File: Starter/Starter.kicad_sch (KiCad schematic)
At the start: 49 parts, among them J1 AudioJack, J2 Speaker, J3 UART1, J4 Pot, J5 Conn_01x08_Pin, J6 GND, J7 DACOUT, SW1 UP, SW2 LEFT, SW3 DOWN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

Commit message: schematic cleaning
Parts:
- removed J1: AudioJack, ECE319K:Jack_3.5mm_CUI_SJ1-3523N_Horizontal, symbol ECE319K:HeadphoneJack
- removed J4: Pot, ECE319K:Testpoint_1x02_P2.54mm, symbol ECE319K:Testpoint
- removed J6: GND, ECE319K:Testpoint_1x02_P2.54mm, symbol ECE319K:Testpoint
- removed TP1: 3.3V, ECE319K:Testpoint_1x02_P2.54mm, symbol ECE319K:Testpoint
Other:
- note removed: "unnecessary test point"
- moved on the sheet: C1, C2, C3, R16, R17

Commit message: fix labels and stuff
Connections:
- net GND: no longer R13.2, R14.2
- net PA12 renamed SDC_CS
- net PA13 renamed TFT_DC
- net PB15 renamed TFT_RST
- net PB6 renamed TFT_CS
- net PB7 renamed SPI_MISO
- net PB8 renamed SPI_MOSI
- net PB9 renamed SPI_SCK
- no-connect marks 0 -> 3
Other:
- note added: "do we even need this?"
- note added: "redo with proper vals"
- note removed: "cant you just use DACOUT label?"
- note removed: "speaker"
- moved on the sheet: J2

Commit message: more stuff
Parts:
- removed H1, H2, H3, H4: ~, ECE319K:MountingHole_4_40, symbol ECE319K:MountingHole
- removed R10: 12k, ECE319K:R_Axial_DIN0204_L3.6mm_D1.6mm_P7.62mm_Horizontal, symbol ECE319K:R_0.125W
- removed R5, R8: 1.5k, ECE319K:R_Axial_DIN0204_L3.6mm_D1.6mm_P7.62mm_Horizontal, symbol ECE319K:R_0.125W
- added H1, H2, H3, H4: MountingHole, symbol Mechanical:MountingHole
- R4: value 1.5k -> 750
- R7: value 1.5k -> 3k
- R9: value 12k -> 6k
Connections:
- net +3V3: now also C4.2; no longer C4.1
- net DACOUT: now also R7.1
- net GND: now also C4.1, R13.2, R14.2; no longer C4.2
- net PA22: no longer J3.3 (C), U2.J3_4 (PA22)
- net PA8: no longer J3.2 (B), U2.J1_4 (PA8)
- net PB0 renamed DAC0
- net PB1 renamed DAC1
- net PB2 renamed DAC2
- net PB3 renamed DAC3
- net PB4 renamed DAC4
- new net UART1_TX: J3.2 (B), U2.J1_4 (PA8)
- new net UART2_RX: J3.3 (C), U2.J3_4 (PA22)
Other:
- note removed: "U1_Tx"
- note removed: "U2_Rx"
- note removed: "redo with proper vals"
- note removed: "why 3v3 not 5?"
- company: The University of Texas at Austin -> Ravi Shah & Alice Di Mauro
- title: Starter Project Spring 2025 -> ECE 319H Final Project
- moved on the sheet: C4, D1, D2, D3, D4, J2, JP1, R1, R11, R12, R13, R14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

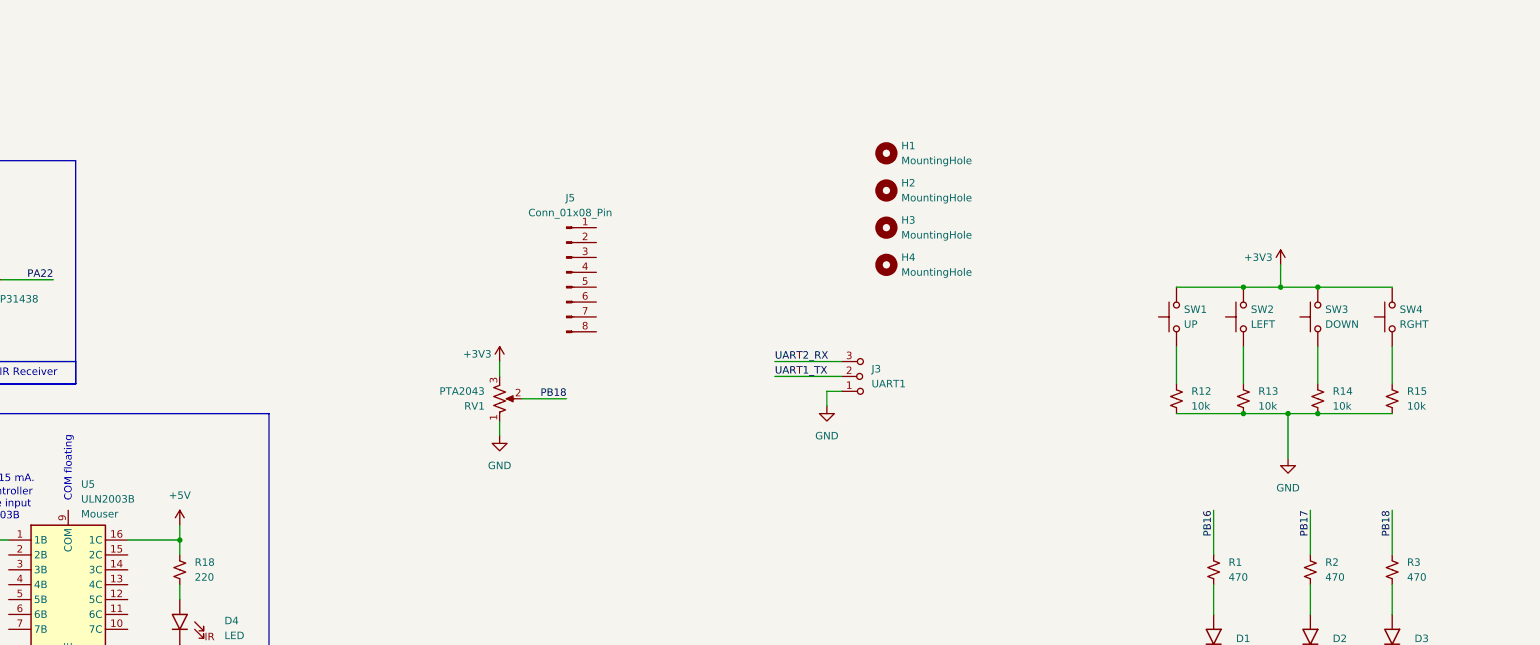
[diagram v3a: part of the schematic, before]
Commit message: add switch debounce
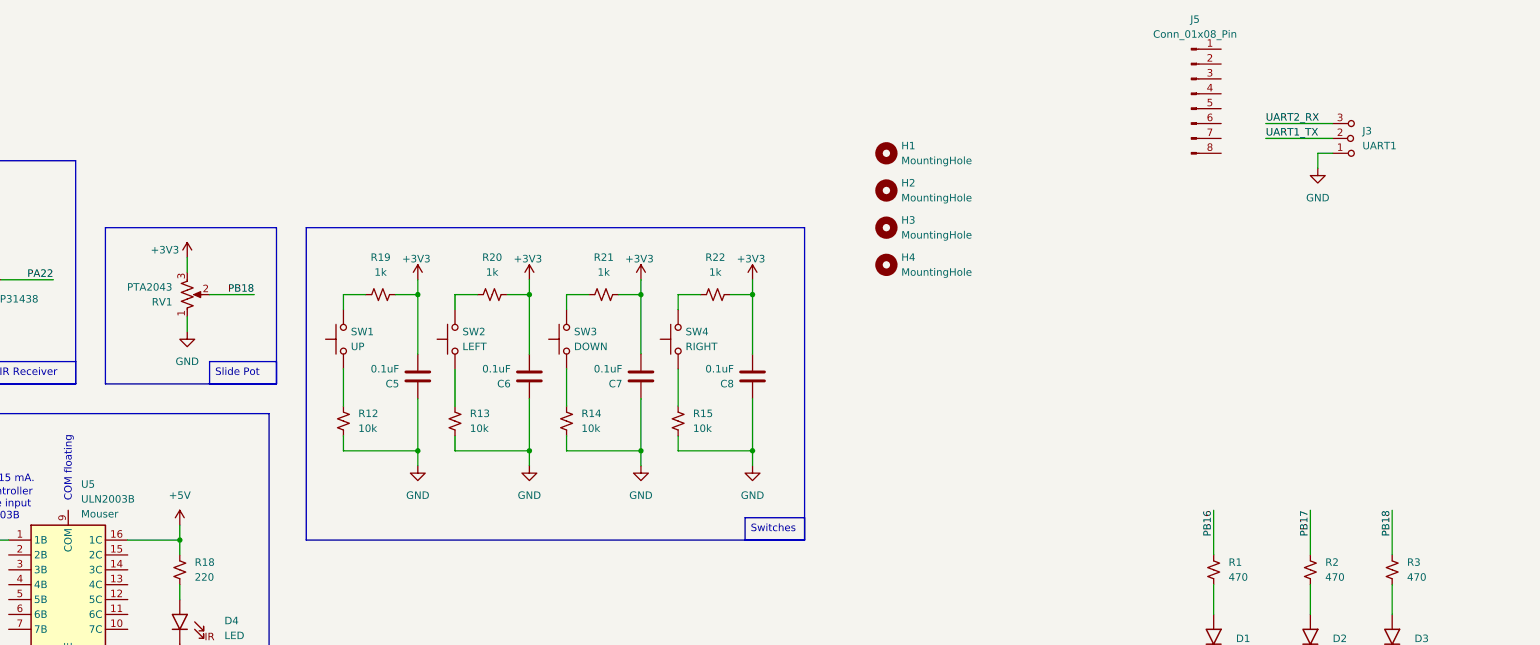
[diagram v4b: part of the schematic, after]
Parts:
- added C5, C6, C7, C8: 0.1uF, ECE319K:C_Axial_200mil, symbol ECE319K:C
- added R19, R20, R21, R22: 1k, ECE319K:R_Axial_DIN0204_L3.6mm_D1.6mm_P7.62mm_Horizontal, symbol ECE319K:R_0.125W
- SW4: value RGHT -> RIGHT
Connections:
- net +3V3: now also C5.2, C6.2, C7.2, C8.2, R19.1, R20.1, R21.1, R22.1; no longer SW1.2, SW2.2, SW3.2, SW4.2
- net GND: now also C5.1, C6.1, C7.1, C8.1
- new net: R19.2, SW1.2
- new net: R21.2, SW3.2
- new net: R22.2, SW4.2
- new net: R20.2, SW2.2
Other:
- moved on the sheet: J3, J5, R12, RV1, SW1

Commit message: speaker amp
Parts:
- removed R17: 10k, ECE319K:R_Axial_DIN0204_L3.6mm_D1.6mm_P7.62mm_Horizontal, symbol ECE319K:R_0.125W
- added D5, D6: LED, ECE319K:LED_D5.0mm, symbol ECE319K:LED
- added R23: 10k, ECE319K:R_Axial_DIN0204_L3.6mm_D1.6mm_P7.62mm_Horizontal, symbol ECE319K:R_0.125W
- added R5: TBD, ECE319K:R_Axial_DIN0204_L3.6mm_D1.6mm_P7.62mm_Horizontal, symbol ECE319K:R_0.125W
- added R8: 470, ECE319K:R_Axial_DIN0204_L3.6mm_D1.6mm_P7.62mm_Horizontal, symbol ECE319K:R_0.125W
- U3: value MCP34119P -> MCP34119D
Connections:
- net +5V: now also U3.6 (Vcc)
- net DACOUT: now also C3.1; no longer J2.1, R11.1, R4.1, R6.1, R7.1, R9.1
- net GND: now also C1.2, C2.2, U3.1 (CD), U3.7 (GND), D5.1 (K), D6.1 (K); no longer J2.2
- net PB16: no longer R1.1
- net PB17: no longer R2.1
- net PB18: no longer R3.1
- net at U3.2 (FC2): now also C2.1
- net at U3.3 (FC1): now also C1.1
- net at U3.4 (VIN): now also R16.1, R23.2
- net at U3.5 (VO1): now also J2.1, R23.1
- net at U3.8 (VO2): now also J2.2
- net at R16.2: now also C3.2
- new net: R11.1, R4.1, R6.1, R7.1, R9.1
- new net: D6.2 (A), R8.2
- new net: D5.2 (A), R5.2
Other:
- note added: "add pins and redo resistor vals based on LED datasheet"
- note removed: "check that these pins are correct?"
- moved on the sheet: C1, C2, C3, C5, C6, C7, C8, D1, D2, D3, H1, H2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

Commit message: IMU
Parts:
- added C10: 2.2nF, ECE319K:C_Axial_200mil, symbol ECE319K:C
- added C11, C9: 0.1uF, ECE319K:C_Axial_200mil, symbol ECE319K:C
- added C12: 10nF, ECE319K:C_Axial_200mil, symbol ECE319K:C
- added R10, R17: 4.7k, ECE319K:R_Axial_DIN0204_L3.6mm_D1.6mm_P7.62mm_Horizontal, symbol ECE319K:R_0.125W
- added U1: MPU-6050, Sensor_Motion:InvenSense_QFN-24_4x4mm_P0.5mm, symbol Sensor_Motion:MPU-6050
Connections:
- net PA24 is gone; now on net DAC4: U2.J3_7 (PA24)
- net PA25 is gone; now on net DAC3: U2.J1_2 (PA25)
- net PA26 is gone; now on net DAC2: U2.J1_5 (PA26)
- net PA27 is gone; now on net DAC1: U2.J1_8 (PA27)
- net PA28 is gone; now on net DAC0: U2.J4_3 (PA28)
- net +3V3: now also C11.1, C12.1, R10.1, R17.1, U1.13 (VDD), U1.8 (VLOGIC)
- net DAC0: no longer U2.J2_9 (PB0)
- net DAC1: no longer U2.J4_2 (PB1)
- net DAC2: no longer U2.J1_9 (PB2)
- net DAC3: no longer U2.J1_10 (PB3)
- net DAC4: no longer U2.J4_1 (PB4)
- net GND: now also C10.2, C11.2, C12.2, C9.2, U1.1 (CLKIN), U1.11 (FSYNC), U1.18 (GND), U1.9 (AD0)
- new net: C9.1, U1.10 (REGOUT)
- new net: C10.1, U1.20 (CPOUT)
- new net I2C_SCL: R17.2, U1.23 (SCL), U2.J1_9 (PB2)
- new net I2C_SDA: R10.2, U1.24 (SDA), U2.J1_10 (PB3)
- no-connect marks 3 -> 6
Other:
- note added: "VDD Bypass"
- note added: "VLogic Bypass"

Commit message: wow im dumb
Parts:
- added C13: 0.1uF, ECE319K:C_Axial_200mil, symbol ECE319H:C
- added D7: 1N4001, Diode_THT:D_DO-41_SOD81_P10.16mm_Horizontal, symbol Diode:1N4001
- added M1: Vibration Motor, symbol Motor:Motor_DC
- added Q1: 2N2222, symbol Simulation_SPICE:NPN
- added R24: 1k, ECE319K:R_Axial_DIN0204_L3.6mm_D1.6mm_P7.62mm_Horizontal, symbol ECE319K:R_0.125W
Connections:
- net PA22 is gone; now on net UART2_RX: U6.3 (Out)
- net PA8 is gone; now on net UART1_TX: U5.1 (1B)
- net +3V3: now also SW1.2, SW2.2, SW3.2, SW4.2, C13.1, D7.1 (K), M1.1 (+); no longer C5.2, C6.2, C7.2, C8.2, R19.1, R20.1, R21.1, R22.1
- net +5V: no longer U5.16 (1C)
- net GND: now also C5.2, C6.2, C7.2, C8.2, Q1.3 (E); no longer C5.1, C6.1, C7.1, C8.1, D4.1 (K)
- net PA15: now also C8.1, R22.1
- net PA16: now also C7.1, R21.1
- net PA17: now also C6.1, R20.1
- net PA18: now also C5.1, R19.1
- net at R13.1, SW2.1: now also R20.2
- net at R19.2: now also R12.1, SW1.1; no longer SW1.2
- net MTR_PWM: now reaches U2.J4_1 (PB4)
- net MTR_PWM: now also R24.1
- net at R21.2: now also R14.1, SW3.1; no longer SW3.2
- net at R15.1, SW4.1: now also R22.2
- net PA10: no longer names the net of U2.J4_7 (PA10)
- net PA11: no longer names the net of U2.J4_8 (PA11)
- net PA31: no longer names the net of U2.J4_4 (PA31)
- net PB12: no longer names the net of U2.J2_2 (PB12)
- net PB13: no longer names the net of U2.J4_6 (PB13)
- net PB16: no longer names the net of U2.J2_10 (PB16)
- net PB17: no longer names the net of U2.J2_3 (PB17)
- net PB19: no longer names the net of U2.J3_3 (PB19)
- net PB23: no longer names the net of U2.J1_3 (PA9/PB23)
- net PB24: no longer names the net of U2.J1_6 (PB24)
- new net: Q1.2 (B), R24.2
- new net: C13.2, D7.2 (A), M1.2 (-), Q1.1 (C)
- new net: D4.1 (K), U5.16 (1C)
- no-connect marks 6 -> 32
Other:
- note added: "I2C Pullups"
- note added: "break out any remaining pins here"
- moved on the sheet: C1, C10, C11, C12, C2, C3, C4, C5, C9, D1, D2, D3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

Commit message: fix leds
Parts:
- C1, C2: footprint ECE319K:CP_Radial_Tantal200mil -> (none)
- C10, C11, C12, C13, C3, C4, C5, C6, C7, C8, C9: footprint ECE319K:C_Axial_200mil -> (none)
- D1, D2, D3, D4, D5, D6: footprint ECE319K:LED_D5.0mm -> (none)
- D7: value 1N4001 -> S1A; footprint Diode_THT:D_DO-41_SOD81_P10.16mm_Horizontal -> (none)
- R1, R10, R11, R12, R13, R14, R15, R16, R17, R18, R19, R2, R20, R21, R22, R23, R24, R3, R4, R6, R7, R8, R9: footprint ECE319K:R_Axial_DIN0204_L3.6mm_D1.6mm_P7.62mm_Horizontal -> (none)
- R5: value TBD -> 470; footprint ECE319K:R_Axial_DIN0204_L3.6mm_D1.6mm_P7.62mm_Horizontal -> (none)
- SW1, SW2, SW3, SW4: footprint ECE319K:SW_PUSH_6mm -> (none)
- U3: footprint ECE319K:DIP-8_W7.62mm_LongPads -> (none)
- U5: footprint ECE319K:DIP-16_W7.62mm -> (none)
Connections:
- net PB17: now reaches R1.1
- net PB17: now also U2.J2_3 (PB17)
- net PB12: now reaches R8.1
- net PB12: now also U2.J2_2 (PB12)
- net PB16: now reaches U2.J2_10 (PB16)
- net PB16: now also R2.1
- net PB19: now reaches U2.J3_3 (PB19)
- net PB19: now also R5.1
- net PB13: now reaches U2.J4_6 (PB13)
- net PB13: now also R3.1
- no-connect marks 32 -> 27
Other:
- moved on the sheet: J5, JP1
